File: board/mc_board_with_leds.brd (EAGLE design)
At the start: 131 x 76.6 mm, 30 parts, among them IC2 MEGA8-P, Q2 16MHz

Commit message: board finished
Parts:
- moved C7 8.35 mm to (39.0, 37.7), turned to 270 degrees
- moved R9 6.87 mm to (49.1, 41.4)
- moved C6 6.48 mm to (55.2, 45.1)
- moved R1 2.90 mm to (67.1, 41.7)
- moved ISP1 2.62 mm to (80.9, 27.2)
- moved IC2 2.08 mm to (57.7, 33.5)
- moved UART1 2.07 mm to (45.0, 40.9)
- moved R6 2.05 mm to (83.3, 34.9), turned to 138.6 degrees
- moved R5 1.98 mm to (48.8, 33.7)
- moved C5 1.78 mm to (59.9, 45.3)
- moved R7 1.73 mm to (33.3, 38.3)
- moved R3 1.62 mm to (71.8, 41.4), turned to 238.6 degrees
- moved R4 1.42 mm to (77.5, 39.0)
- moved R10 0.85 mm to (53.8, 40.8), turned to 269.6 degrees
- moved R8 0.68 mm to (37.8, 42.0)
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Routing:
- net GND: track 211.5 -> 188.4 mm
- net N$15: track 47.6 -> 34.3 mm
- net PD3/LED7: track 12.8 -> 3.97 mm
- net +5V: track 114.9 -> 109.2 mm
- net PD5/LED1: track 8.87 -> 3.55 mm
- net N$11: track 3.62 -> 8.73 mm
- net PC1/SCK: track 53.4 -> 48.5 mm
- net PC0/DT: track 52.1 -> 47.7 mm
- net PD6/LED2: track 8.00 -> 4.16 mm
- net N$7: track 3.59 -> 7.29 mm
- net PB3/MOSI: track 15.4 -> 19.0 mm
- net N$14: track 16.3 -> 13.4 mm
- net PD4/LED8: track 5.42 -> 2.56 mm
- net PB5/SCK: track 18.5 -> 21.0 mm
- net N$4: track 13.4 -> 11.2 mm
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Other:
- board text removed: "ISP"
- board text removed: "LED 1 2 3 4"

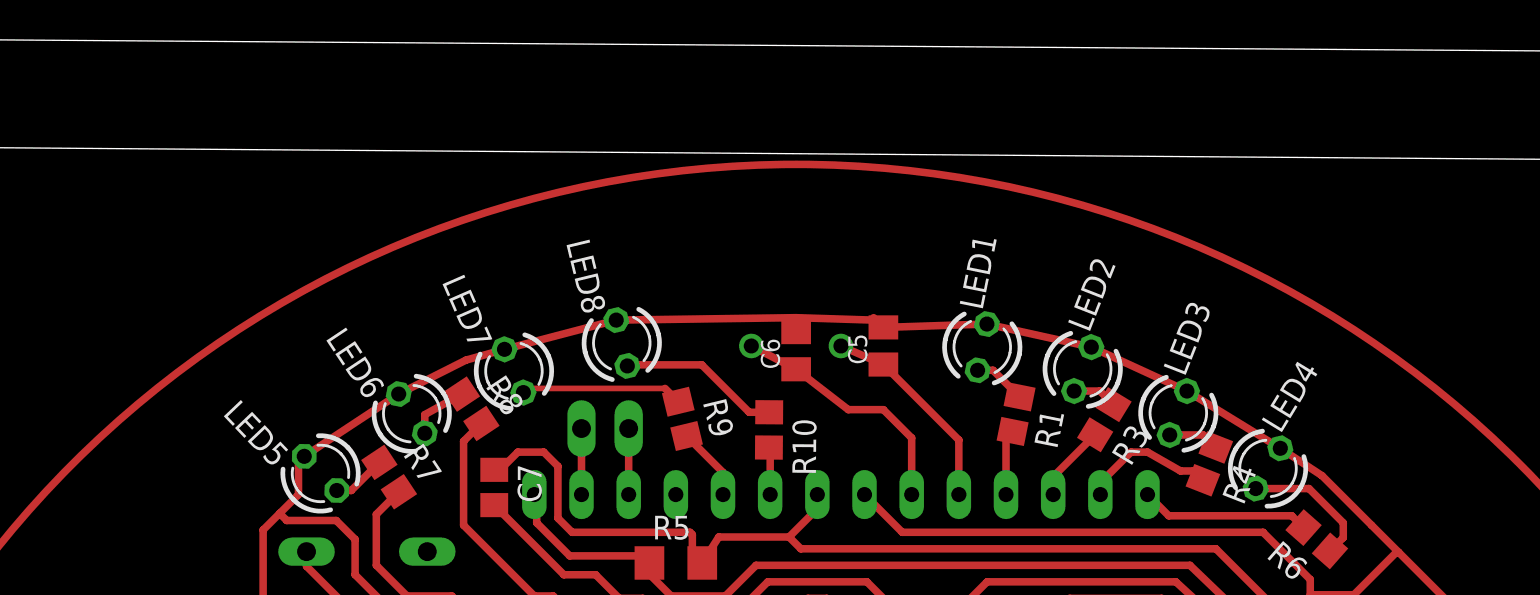
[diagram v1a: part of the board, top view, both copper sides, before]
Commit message: renamed LEDs in .c file and schematic
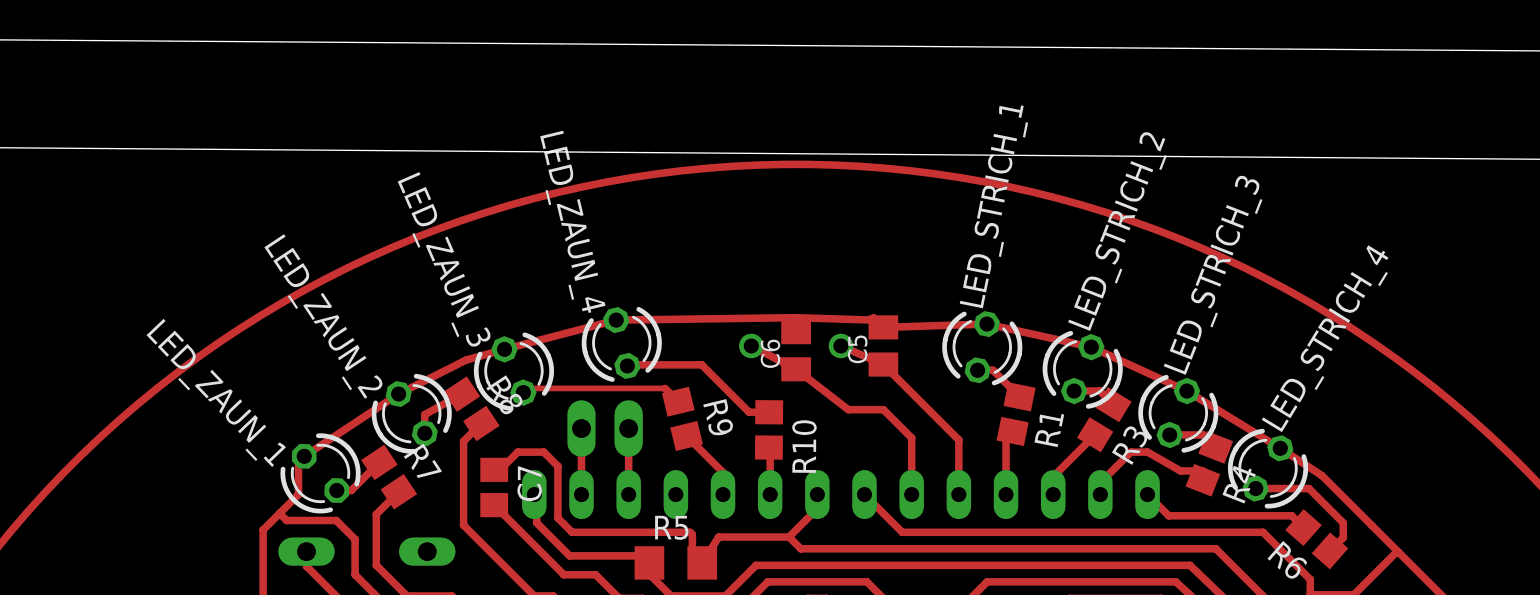
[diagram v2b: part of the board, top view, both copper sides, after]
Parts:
- renumbered LED1 to LED_STRICH_1, LED2 to LED_STRICH_2, LED3 to LED_STRICH_3, LED4 to LED_STRICH_4, LED5 to LED_ZAUN_1, LED6 to LED_ZAUN_2, LED7 to LED_ZAUN_3, LED8 to LED_ZAUN_4
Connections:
- net PB0/LED4 renamed PB0/LED_STRICH_4
- net PC4/LED6 renamed PC4/LED_ZAUN_2
- net PC5/LED5 renamed PC5/LED_ZAUN_1
- net PD3/LED7 renamed PD3/LED_ZAUN_3
- net PD4/LED8 renamed PD4/LED_ZAUN_4
- net PD5/LED1 renamed PD5/LED_STRICH_1
- net PD6/LED2 renamed PD6/LED_STRICH_2
- net PD7/LED3 renamed PD7/LED_STRICH_3
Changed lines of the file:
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@@
 </autorouter>
 <elements>
-<element name="LED1" library="led" package="LED3MM" value="" x="65.26883125" y="45.27481875" rot="R78.6"/>
-<element name="LED2" library="led" package="LED3MM" value="" x="70.6780875" y="44.09545625" rot="R68.6"/>
-<element name="LED3" library="led" package="LED3MM" value="" x="75.826471875" y="41.72945625" rot="R68.6"/>
-<element name="LED4" library="led" package="LED3MM" value="" x="80.6571" y="38.7449125" rot="R58.6"/>
-<element name="LED5" library="led" package="LED3MM" value="" x="29.6350125" y="38.4763" rot="R133.6"/>
-<element name="LED6" library="led" package="LED3MM" value="" x="34.5460125" y="41.69431875" rot="R123.6"/>
-<element name="LED7" library="led" package="LED3MM" value="" x="40.04930625" y="43.994065625" rot="R113.6"/>
-<element name="LED8" library="led" package="LED3MM" value="" x="45.85698125" y="45.498234375" rot="R103.6"/>
+<element name="LED_STRICH_1" library="led" package="LED3MM" value="" x="65.26883125" y="45.27481875" rot="R78.6"/>
+<element name="LED_STRICH_2" library="led" package="LED3MM" value="" x="70.6780875" y="44.09545625" rot="R68.6"/>
+<element name="LED_STRICH_3" library="led" package="LED3MM" value="" x="75.826471875" y="41.72945625" rot="R68.6"/>
+<element name="LED_STRICH_4" library="led" package="LED3MM" value="" x="80.6571" y="38.7449125" rot="R58.6"/>
+<element name="LED_ZAUN_1" library="led" package="LED3MM" value="" x="29.6350125" y="38.4763" rot="R133.6"/>
+<element name="LED_ZAUN_2" library="led" package="LED3MM" value="" x="34.5460125" y="41.69431875" rot="R123.6"/>
+<element name="LED_ZAUN_3" library="led" package="LED3MM" value="" x="40.04930625" y="43.994065625" rot="R113.6"/>
+<element name="LED_ZAUN_4" library="led" package="LED3MM" value="" x="45.85698125" y="45.498234375" rot="R103.6"/>
 <element name="R1" library="resistor" package="R0805" value="470" x="67.091109375" y="41.668040625" rot="R258.6"/>
 <element name="R3" library="resistor" package="R0805" value="470" x="71.842928125" y="41.36911875" rot="R238.6"/>
@@
 </signal>
 <signal name="GND">
-<contactref element="LED1" pad="K"/>
-<contactref element="LED2" pad="K"/>
-<contactref element="LED3" pad="K"/>
-<contactref element="LED4" pad="K"/>
-<contactref element="LED5" pad="K"/>
-<contactref element="LED6" pad="K"/>
-<contactref element="LED7" pad="K"/>
-<contactref element="LED8" pad="K"/>
+<contactref element="LED_STRICH_1" pad="K"/>
+<contactref element="LED_STRICH_2" pad="K"/>
+<contactref element="LED_STRICH_3" pad="K"/>
+<contactref element="LED_STRICH_4" pad="K"/>
+<contactref element="LED_ZAUN_1" pad="K"/>
+<contactref element="LED_ZAUN_2" pad="K"/>
+<contactref element="LED_ZAUN_3" pad="K"/>
+<contactref element="LED_ZAUN_4" pad="K"/>
 <contactref element="PWRLED" pad="K"/>
 <contactref element="IC2" pad="8"/>
@@
 <contactref element="IC2" pad="16"/>
 </signal>
-<signal name="PD5/LED1">
-<contactref element="IC2" pad="11"/>
-<contactref element="R1" pad="2"/>
-<wire x1="66.903334375" y1="40.73678125" x2="66.548" y2="40.381446875" width="0.4064" layer="1"/>
-<wire x1="66.548" y1="40.381446875" x2="66.548" y2="37.338" width="0.4064" layer="1"/>
-</signal>
-<signal name="PD3/LED7">
+<signal name="PD3/LED_ZAUN_3">
 <contactref element="IC2" pad="5"/>
 <contactref element="R9" pad="2"/>
@@
 <wire x1="51.308" y1="38.52985" x2="49.34691875" y2="40.49093125" width="0.4064" layer="1"/>
 </signal>
-<signal name="PD4/LED8">
+<signal name="PD4/LED_ZAUN_4">
 <contactref element="IC2" pad="6"/>
 <contactref element="R10" pad="2"/>
 <wire x1="53.848" y1="37.338" x2="53.848" y2="39.8033375" width="0.4064" layer="1"/>
 <wire x1="53.848" y1="39.8033375" x2="53.78190625" y2="39.86943125" width="0.4064" layer="1" curve="90"/>
-</signal>
-<signal name="PD7/LED3">
-<contactref element="IC2" pad="13"/>
-<contactref element="R4" pad="2"/>
-<wire x1="77.1496625" y1="38.107846875" x2="76.649509375" y2="38.608" width="0.4064" layer="1"/>
-<wire x1="76.649509375" y1="38.608" x2="75.946" y2="38.608" width="0.4064" layer="1"/>
-<wire x1="75.946" y1="38.608" x2="74.168" y2="39.624" width="0.4064" layer="1"/>
-<wire x1="74.168" y1="39.624" x2="73.279" y2="39.624" width="0.4064" layer="1"/>
-<wire x1="73.279" y1="39.624" x2="71.628" y2="37.973" width="0.4064" layer="1"/>
-<wire x1="71.628" y1="37.973" x2="71.628" y2="37.338" width="0.4064" layer="1"/>
 </signal>
 <signal name="PC0/DT">
@@
 <wire x1="28.8798" y1="33.4772" x2="28.8798" y2="34.2646" width="0.4064" layer="1"/>
 </signal>
-<signal name="PD6/LED2">
-<contactref element="IC2" pad="12"/>
-<contactref element="R3" pad="2"/>
-<wire x1="71.34796875" y1="40.55824375" x2="69.088" y2="38.298275" width="0.4064" layer="1"/>
-<wire x1="69.088" y1="38.298275" x2="69.088" y2="37.338" width="0.4064" layer="1"/>
-</signal>
 <signal name="RESET">
 <contactref element="IC2" pad="1"/>
@@
 <wire x1="46.228" y1="37.338" x2="46.228" y2="40.894" width="0.4064" layer="1"/>
 </signal>
-<signal name="PC5/LED5">
+<signal name="PC5/LED_ZAUN_1">
 <contactref element="IC2" pad="28"/>
 <contactref element="R7" pad="2"/>
@@
 <wire x1="32.639" y1="36.27205625" x2="33.855384375" y2="37.488440625" width="0.4064" layer="1"/>
 </signal>
-<signal name="PC4/LED6">
+<signal name="PC4/LED_ZAUN_2">
 <contactref element="IC2" pad="27"/>
 <contactref element="R8" pad="2"/>
@@
 <signal name="N$1">
 <contactref element="R1" pad="1"/>
-<contactref element="LED1" pad="A"/>
+<contactref element="LED_STRICH_1" pad="A"/>
 <wire x1="67.27888125" y1="42.599296875" x2="65.84830625" y2="44.029871875" width="0.4064" layer="1"/>
 <wire x1="65.84830625" y1="44.029871875" x2="65.01780625" y2="44.029871875" width="0.4064" layer="1"/>
@@
 <signal name="N$2">
 <contactref element="R3" pad="1"/>
-<contactref element="LED2" pad="A"/>
+<contactref element="LED_STRICH_2" pad="A"/>
 <wire x1="72.337884375" y1="42.179990625" x2="71.6048625" y2="42.9130125" width="0.4064" layer="1"/>
 <wire x1="71.6048625" y1="42.9130125" x2="70.21469375" y2="42.9130125" width="0.4064" layer="1"/>
@@
 <signal name="N$3">
 <contactref element="R4" pad="1"/>
-<contactref element="LED3" pad="A"/>
+<contactref element="LED_STRICH_3" pad="A"/>
 <wire x1="77.842928125" y1="39.87685" x2="77.172765625" y2="40.5470125" width="0.4064" layer="1"/>
 <wire x1="77.172765625" y1="40.5470125" x2="75.363078125" y2="40.5470125" width="0.4064" layer="1"/>
@@
 <signal name="N$7">
 <contactref element="R6" pad="1"/>
-<contactref element="LED4" pad="A"/>
+<contactref element="LED_STRICH_4" pad="A"/>
 <wire x1="83.99415625" y1="34.30281875" x2="84.709" y2="35.0176625" width="0.4064" layer="1"/>
 <wire x1="84.709" y1="35.0176625" x2="84.709" y2="35.814" width="0.4064" layer="1"/>
@@
 <signal name="N$8">
 <contactref element="R7" pad="1"/>
-<contactref element="LED5" pad="A"/>
+<contactref element="LED_ZAUN_1" pad="A"/>
 <wire x1="30.510828125" y1="37.5566" x2="31.28954375" y2="37.5566" width="0.4064" layer="1"/>
 <wire x1="31.28954375" y1="37.5566" x2="32.8039375" y2="39.07099375" width="0.4064" layer="1"/>
@@
 <signal name="N$10">
 <contactref element="R8" pad="1"/>
-<contactref element="LED6" pad="A"/>
+<contactref element="LED_ZAUN_2" pad="A"/>
 <wire x1="37.2447625" y1="42.748709375" x2="35.24881875" y2="41.641765625" width="0.4064" layer="1"/>
 <wire x1="35.24881875" y1="41.641765625" x2="35.24881875" y2="40.63650625" width="0.4064" layer="1"/>
@@
 <signal name="N$11">
 <contactref element="R9" pad="1"/>
-<contactref element="LED7" pad="A"/>
+<contactref element="LED_ZAUN_3" pad="A"/>
 <wire x1="48.900146875" y1="42.337659375" x2="48.18480625" y2="43.053" width="0.4064" layer="1"/>
 <wire x1="48.18480625" y1="43.053" x2="40.7804625" y2="43.053" width="0.3048" layer="1"/>
@@
 <signal name="N$12">
 <contactref element="R10" pad="1"/>
-<contactref element="LED8" pad="A"/>
+<contactref element="LED_ZAUN_4" pad="A"/>
 <wire x1="53.795171875" y1="41.769384375" x2="52.718615625" y2="41.769384375" width="0.4064" layer="1"/>
 <wire x1="52.718615625" y1="41.769384375" x2="50.165" y2="44.323" width="0.4064" layer="1"/>
@@
 <wire x1="42.738" y1="33.02" x2="38.989" y2="36.769" width="0.4064" layer="1"/>
 </signal>
-<signal name="PB0/LED4">
+<signal name="PB0/LED_STRICH_4">
 <contactref element="IC2" pad="14"/>
 <contactref element="R6" pad="2"/>
@@
 <contactref element="IC2" pad="15"/>
 </signal>
+<signal name="PD5/LED_STRICH_1">
+<contactref element="R1" pad="2"/>
+<contactref element="IC2" pad="11"/>
+<wire x1="66.548" y1="40.381446875" x2="66.548" y2="37.338" width="0.4064" layer="1"/>
+<wire x1="66.548" y1="40.381446875" x2="66.903334375" y2="40.381446875" width="0.4064" layer="1"/>
+<wire x1="66.903334375" y1="40.381446875" x2="66.903334375" y2="40.73678125" width="0.4064" layer="1"/>
+</signal>
+<signal name="PD6/LED_STRICH_2">
+<contactref element="R3" pad="2"/>
+<contactref element="IC2" pad="12"/>
+<wire x1="69.088" y1="38.298275" x2="69.088" y2="37.338" width="0.4064" layer="1"/>
+<wire x1="69.088" y1="38.298275" x2="71.34796875" y2="40.55824375" width="0.4064" layer="1"/>
+</signal>
+<signal name="PD7/LED_STRICH_3">
+<contactref element="R4" pad="2"/>
+<contactref element="IC2" pad="13"/>
+<wire x1="75.946" y1="38.608" x2="74.168" y2="39.624" width="0.4064" layer="1"/>
+<wire x1="74.168" y1="39.624" x2="73.279" y2="39.624" width="0.4064" layer="1"/>
+<wire x1="73.279" y1="39.624" x2="71.628" y2="37.973" width="0.4064" layer="1"/>
+<wire x1="71.628" y1="37.973" x2="71.628" y2="37.338" width="0.4064" layer="1"/>
+<wire x1="75.946" y1="38.608" x2="77.1496625" y2="38.608" width="0.4064" layer="1"/>
+<wire x1="77.1496625" y1="38.608" x2="77.1496625" y2="38.107846875" width="0.4064" layer="1"/>
+</signal>
 </signals>
